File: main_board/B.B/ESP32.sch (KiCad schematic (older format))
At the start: 37 parts, among them J5 USB_C_Receptacle_USB2.0, Q3 AO3400A, SW1 SW_DIP_x01, SW2 SW_DIP_x01, SW4 SW_DIP_x02, U64 CP2102N-A01-GQFN28, U65 ESP32-WROVER

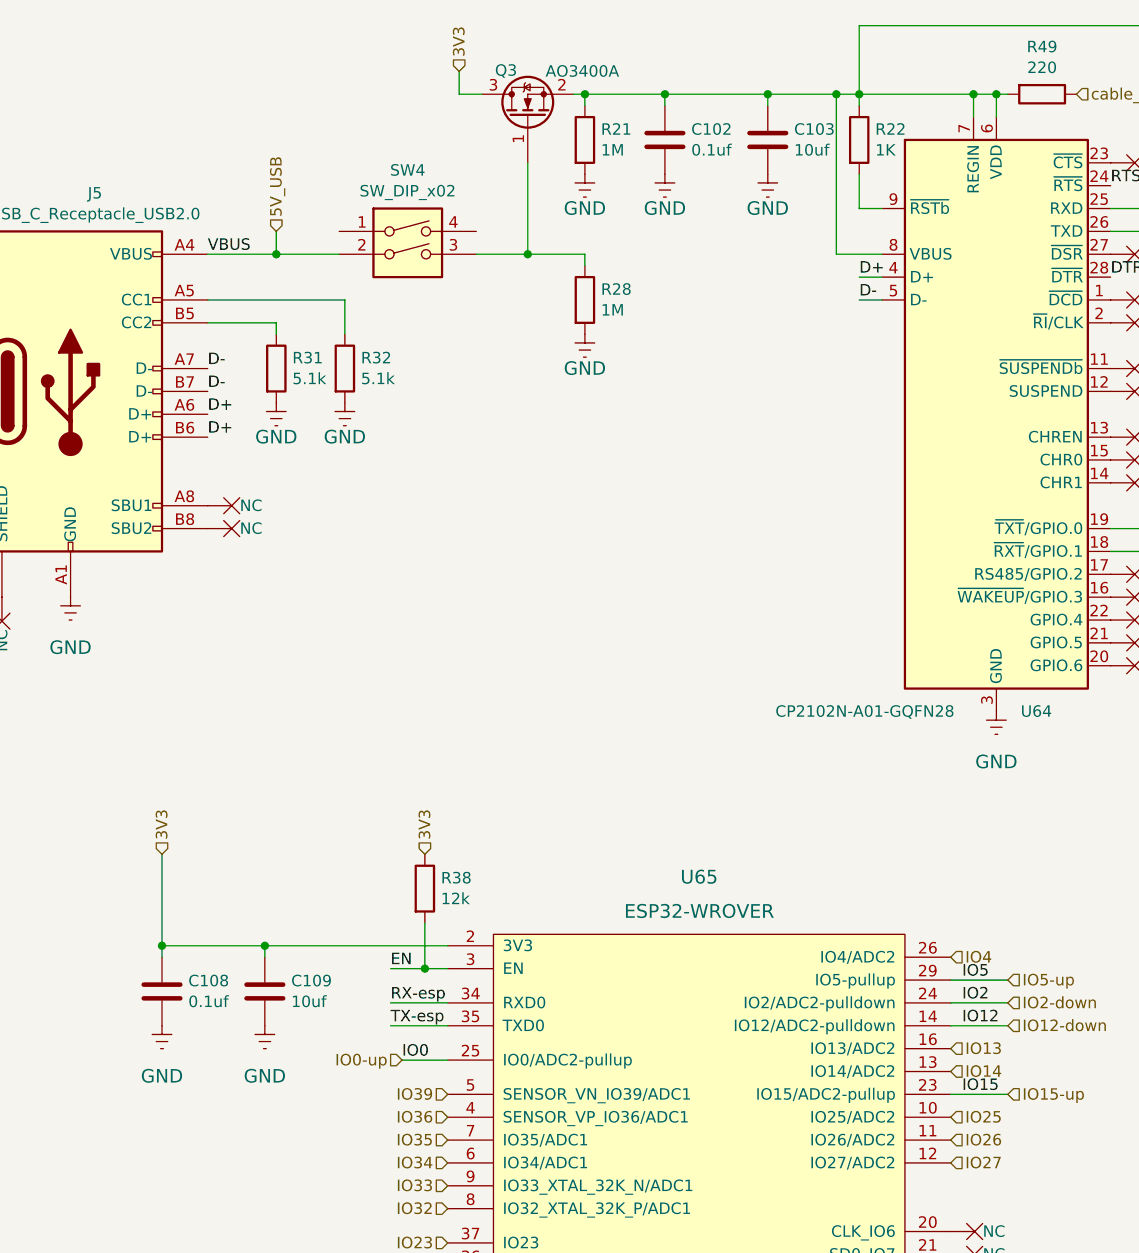
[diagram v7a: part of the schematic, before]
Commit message: JLCdata
- korekce pozice a natoceni
- data pro vyrobu
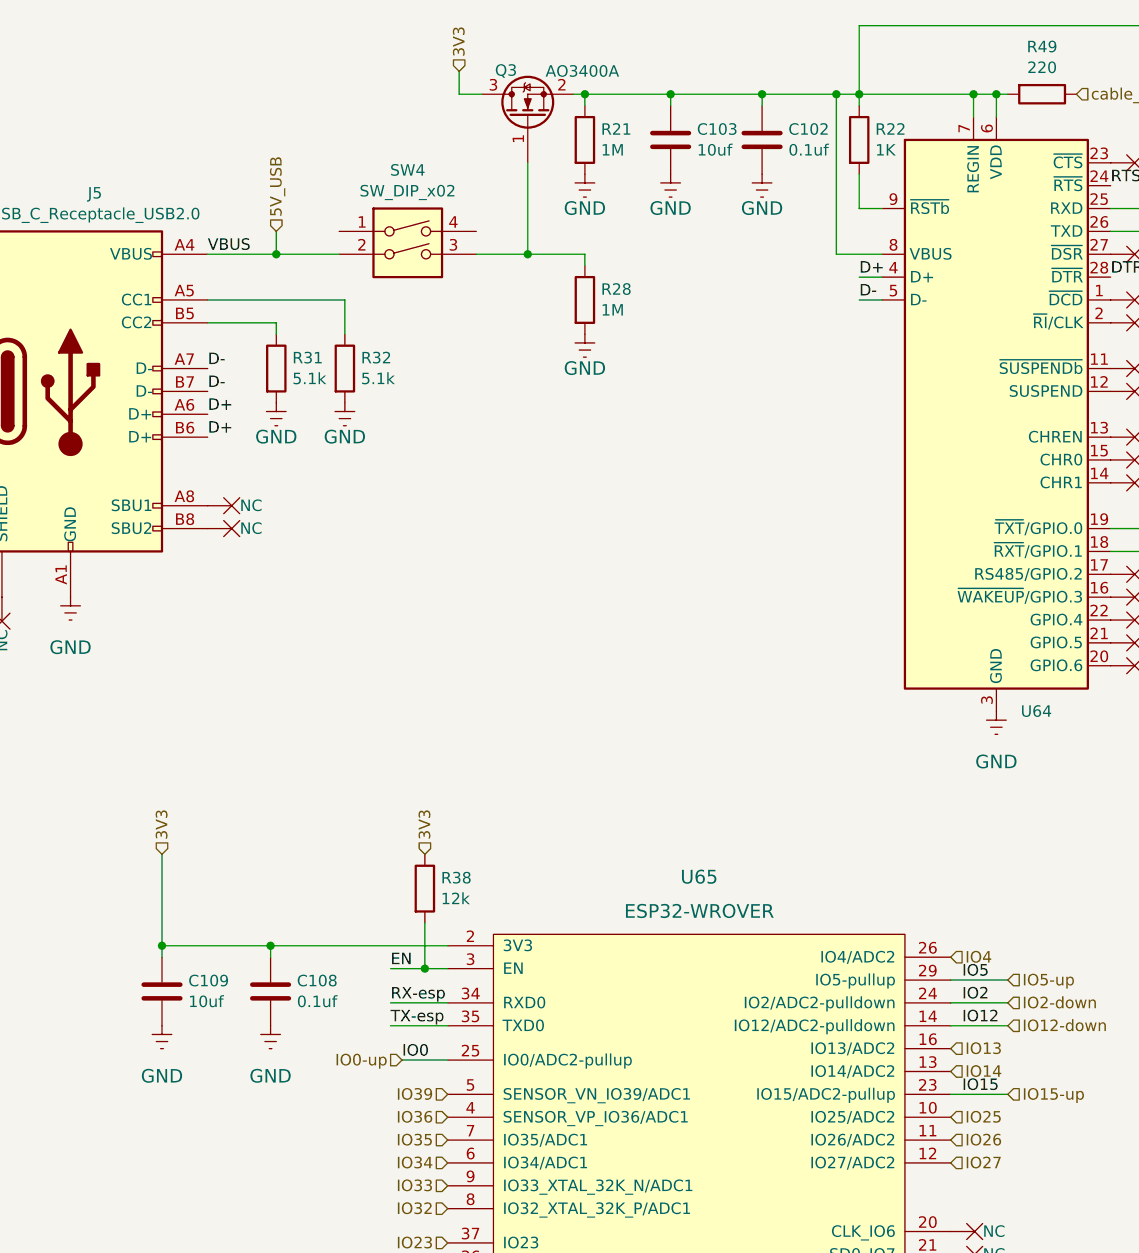
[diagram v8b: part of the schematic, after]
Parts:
- C102, C108: LCSC C14663 -> C49678
- MMBT1: Field5 (none) -> C115751; JLCPCB_CORRECTION (none) -> 0;0;180
- MMBT3904, Q3: JLCPCB_CORRECTION (none) -> 0;0;180
- U64: JLCPCB_CORRECTION (none) -> 0;0;-90
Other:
- moved on the sheet: C103, C108, C109
